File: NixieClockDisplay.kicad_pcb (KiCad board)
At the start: 2 copper layers, 160 x 65 mm, 54 parts, among them U1 TPIC6B595, U2 TPIC6B595, U3 TPIC6B595, U4 TPIC6B595, U5 TPIC6B595, U6 TPIC6B595, U7 WE-FDSM_DC/DC_5V

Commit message: Fiddling.
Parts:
- moved C11 16.0 mm to (130.0, 60.0), turned to 90 degrees
- moved C12 16.0 mm to (170.0, 60.0), turned to 90 degrees
- moved C15 16.0 mm to (180.0, 60.0), turned to 90 degrees
- moved C16 16.0 mm to (220.0, 60.0), turned to 90 degrees
- moved C8 16.0 mm to (120.0, 60.0), turned to 270 degrees
- moved C7 9.62 mm to (80.0, 60.0)
- moved R7 3.40 mm to (78.0, 66.8)
- moved N1 0.36 mm to (90.0, 60.0)
- moved N2 0.36 mm to (110.0, 60.0)
- moved N3 0.36 mm to (140.0, 60.0)
- moved N4 0.36 mm to (160.0, 60.0)
- moved N5 0.36 mm to (190.0, 60.0)
- moved N6 0.36 mm to (210.0, 60.0)
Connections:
- net Net-(J2-Pad1) renamed /HV
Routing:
- net Net-(LED1-Pad3): track 13.7 -> 0.00 mm
- net Net-(N6-Pad1): track 0.00 -> 4.08 mm
- net Net-(N5-Pad1): track 0.00 -> 4.08 mm
- net Net-(N4-Pad1): track 0.00 -> 4.08 mm
- net Net-(N3-Pad1): track 0.00 -> 4.08 mm
- net Net-(N2-Pad1): track 0.00 -> 4.08 mm
- net Net-(N1-Pad1): track 0.00 -> 4.08 mm
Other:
- net class Default: clearance 0.2 -> 0.25
- net class HV added: clearance 2, trace_width 1, via_dia 2, via_drill 1.5
- rule trace_clearance: 0.2 -> 0.25

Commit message: More layout
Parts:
- moved C11 10.3 mm to (140.0, 62.5), turned to 180 degrees
- moved C12 10.3 mm to (160.0, 62.5), turned to 180 degrees
- moved C15 10.3 mm to (190.0, 62.5), turned to 180 degrees
- moved C16 10.3 mm to (210.0, 62.5), turned to 180 degrees
- moved C7 10.3 mm to (90.0, 62.5), turned to 180 degrees
- moved C8 10.3 mm to (110.0, 62.5), turned to 180 degrees
- moved R7 7.65 mm to (79.5, 59.2)
- moved C14 2.00 mm to (175.0, 70.0), turned to 180 degrees
- moved LED8 2.00 mm to (175.0, 65.0), turned to 180 degrees
- moved C10 1.00 mm to (125.0, 70.0), turned to 180 degrees
- moved LED1 0.75 mm to (90.0, 59.2), turned to 180 degrees
- moved LED10 0.75 mm to (210.0, 59.2), turned to 180 degrees
- moved LED2 0.75 mm to (110.0, 59.2), turned to 180 degrees
- moved LED5 0.75 mm to (140.0, 59.2), turned to 180 degrees
- moved LED6 0.75 mm to (160.0, 59.2), turned to 180 degrees
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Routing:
- net +5V: track 0.00 -> 60.7 mm
- net GND: track 0.00 -> 58.2 mm
- net Net-(LED6-Pad1): track 0.00 -> 32.6 mm
- net Net-(LED5-Pad1): track 0.00 -> 20.3 mm
- net Net-(LED10-Pad3): track 0.00 -> 20.3 mm
- net Net-(LED1-Pad1): track 0.00 -> 20.3 mm
- net Net-(LED8-Pad1): track 0.00 -> 16.0 mm
- net Net-(LED4-Pad1): track 0.00 -> 16.0 mm
- net Net-(LED1-Pad3): track 0.00 -> 9.20 mm
- net Net-(LED7-Pad1): track 0.00 -> 7.49 mm
- net Net-(LED3-Pad1): track 0.00 -> 7.49 mm

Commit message: Moar traces
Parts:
- moved R2 15.4 mm to (107.5, 90.0)
- moved R1 15.2 mm to (87.5, 90.0)
- moved C1 5.53 mm to (81.2, 80.0)
- moved C2 5.01 mm to (101.2, 80.0)
- moved U1 5.00 mm to (90.0, 80.0), turned to 90 degrees
- moved U2 5.00 mm to (110.0, 80.0), turned to 90 degrees
- turned U3 to 180 degrees
- turned U4 to 180 degrees
- turned U5 to 180 degrees
- turned U6 to 180 degrees
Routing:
- net GND: track 58.2 -> 86.0 mm, vias 0 -> 16
- net /HOUR_00: track 0.00 -> 22.0 mm, vias 0 -> 1
- net /HOUR_20: track 0.00 -> 17.2 mm
- net Net-(LED6-Pad1): track 32.6 -> 16.3 mm
- net Net-(LED2-Pad1): track 0.00 -> 16.3 mm
- net /HOUR_10: track 0.00 -> 10.8 mm
- added copper zone on B.Cu, net GND
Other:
- net class HV: clearance 2 -> 1

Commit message: More layout
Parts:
- moved R4 11.5 mm to (158.8, 90.0), turned to 0 degrees
- moved R3 10.6 mm to (137.5, 90.0), turned to 0 degrees
- moved R5 10.6 mm to (187.5, 90.0), turned to 0 degrees
- moved R6 10.6 mm to (207.5, 90.0), turned to 0 degrees
- moved C4 10.1 mm to (151.2, 80.0), turned to 270 degrees
- moved C5 10.1 mm to (181.2, 80.0), turned to 270 degrees
- moved C6 10.1 mm to (201.2, 80.0), turned to 270 degrees
- moved C3 9.74 mm to (131.2, 80.0), turned to 270 degrees
- moved U3 4.00 mm to (140.0, 80.0), turned to 90 degrees
- moved U4 4.00 mm to (160.0, 80.0), turned to 90 degrees
- moved U5 4.00 mm to (190.0, 80.0), turned to 90 degrees
- moved U6 4.00 mm to (210.0, 80.0), turned to 90 degrees
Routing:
- net /HOUR_9: track 0.00 -> 38.5 mm, vias 0 -> 1
- net /HOUR_0: track 0.00 -> 26.2 mm, vias 0 -> 1
- net +5V: track 60.7 -> 71.8 mm
- net Net-(R2-Pad2): track 0.00 -> 8.94 mm
- net Net-(R1-Pad2): track 0.00 -> 8.94 mm
- removed copper zone on B.Cu, net GND

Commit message: More layout
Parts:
- added J1: CONN_01X08, Pin_Headers:Pin_Header_Angled_1x08_Pitch2.54mm, B.Cu at (129.5, 94.8)
- added J2: CONN_01X03, Pin_Headers:Pin_Header_Angled_1x03_Pitch2.54mm, B.Cu at (152.4, 94.7)
- added J3: CONN_01X03, Pin_Headers:Pin_Header_Angled_1x03_Pitch2.54mm, B.Cu at (162.6, 94.7)
- U7: moved to B.Cu
- moved U7 32.2 mm to (120.2, 92.5), turned to 180 degrees
- moved R10 24.4 mm to (198.0, 45.6), turned to 90 degrees
- moved R11 24.4 mm to (118.0, 45.6), turned to 90 degrees
- moved R12 24.4 mm to (168.0, 45.6), turned to 90 degrees
- moved R8 24.4 mm to (98.0, 45.6), turned to 90 degrees
- moved R9 24.4 mm to (148.0, 45.6), turned to 90 degrees
- moved R13 20.6 mm to (218.0, 49.4), turned to 90 degrees
- moved R4 2.80 mm to (157.5, 87.5)
- moved R1 2.50 mm to (87.5, 87.5)
- moved R2 2.50 mm to (107.5, 87.5)
- moved R3 2.50 mm to (137.5, 87.5)
- moved R5 2.50 mm to (187.5, 87.5)
- moved R6 2.50 mm to (207.5, 87.5)
- moved C5 1.37 mm to (181.1, 81.4), turned to 90 degrees
- moved C3 1.35 mm to (131.1, 81.3), turned to 90 degrees
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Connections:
- U6 pad 3: /DIN -> Net-(J1-Pad8)
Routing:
- net /HV: track 0.00 -> 237.1 mm
- net +5V: track 71.8 -> 241.9 mm, vias 0 -> 2
- net //G: track 0.00 -> 166.1 mm
- net GND: track 86.0 -> 127.3 mm, vias 16 -> 40
- net /HOUR_9: track 38.5 -> 0.00 mm, vias 1 -> 0
- net +12V: track 0.00 -> 35.5 mm
- net /HOUR_0: track 26.2 -> 0.19 mm, vias 1 -> 0
- net /HOUR_00: track 21.9 -> 0.00 mm, vias 1 -> 0
- net Net-(R6-Pad2): track 0.00 -> 6.88 mm
- net Net-(R5-Pad2): track 0.00 -> 6.88 mm
- net Net-(R4-Pad2): track 0.00 -> 6.88 mm
- net Net-(R3-Pad2): track 0.00 -> 6.88 mm
- net Net-(N6-Pad1): track 4.08 -> 0.00 mm
- net Net-(N5-Pad1): track 4.08 -> 0.00 mm
- net Net-(N4-Pad1): track 4.08 -> 0.00 mm
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- added copper zone on B.Cu, net GND

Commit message: Rotating driver chips
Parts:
- removed REF** (x2): MountingHole_3.7mm, Mounting_Holes:MountingHole_3.7mm
- moved C5 22.1 mm to (198.8, 94.6), turned to 270 degrees
- moved C6 21.4 mm to (218.8, 93.5)
- moved R6 13.5 mm to (221.0, 88.2), turned to 90 degrees
- moved R5 12.5 mm to (200.0, 88.2), turned to 90 degrees
- moved U5 7.50 mm to (190.1, 87.5), turned to 180 degrees
- moved U6 7.50 mm to (210.0, 87.5), turned to 180 degrees
- moved C1 5.25 mm to (81.0, 86.5)
- moved C2 5.25 mm to (100.9, 86.5)
- moved C3 5.25 mm to (131.1, 86.6)
- moved C4 5.25 mm to (150.9, 86.5)
- moved J1 5.25 mm to (129.5, 100.0)
- moved J2 5.25 mm to (152.4, 100.0)
- moved J3 5.25 mm to (162.6, 100.0)
- moved R1 5.25 mm to (87.5, 92.8)
- moved R2 5.25 mm to (107.5, 92.8)
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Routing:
- net +5V: track 241.9 -> 104.5 mm, vias 2 -> 3
- net /HV: track 237.1 -> 328.0 mm
- net /SEC_7: track 0.00 -> 49.7 mm, vias 0 -> 1
- net /SEC_3: track 0.00 -> 31.4 mm, vias 0 -> 2
- net //G: track 166.1 -> 135.7 mm, vias 0 -> 1
- net /SEC_0: track 0.00 -> 29.2 mm, vias 0 -> 1
- net Net-(N1-Pad1): track 0.00 -> 29.0 mm, vias 0 -> 2
- net Net-(N2-Pad1): track 0.00 -> 29.0 mm, vias 0 -> 2
- net Net-(N6-Pad1): track 0.00 -> 29.0 mm, vias 0 -> 2
- net Net-(N5-Pad1): track 0.00 -> 29.0 mm, vias 0 -> 2
- net Net-(N4-Pad1): track 0.00 -> 29.0 mm, vias 0 -> 2
- net Net-(N3-Pad1): track 0.00 -> 29.0 mm, vias 0 -> 2
- net /SEC_2: track 0.00 -> 28.9 mm, vias 0 -> 1
- net /SEC_1: track 0.00 -> 27.1 mm, vias 0 -> 1
- net GND: track 127.3 -> 119.7 mm, vias 40 -> 32
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
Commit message: Much routing
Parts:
- moved C2 17.1 mm to (115.0, 96.2), turned to 0 degrees
- moved C4 17.1 mm to (165.0, 96.2), turned to 0 degrees
- moved C1 17.1 mm to (95.0, 96.2), turned to 0 degrees
- moved C3 16.9 mm to (145.0, 96.2), turned to 0 degrees
- moved R1 12.5 mm to (100.0, 92.5), turned to 90 degrees
- moved R2 12.5 mm to (120.0, 92.5), turned to 90 degrees
- moved R3 12.5 mm to (150.0, 92.5), turned to 90 degrees
- moved R4 12.5 mm to (170.0, 92.5), turned to 90 degrees
- moved C6 4.65 mm to (215.0, 96.2), turned to 0 degrees
- moved R6 4.37 mm to (220.0, 92.5)
- moved R5 4.25 mm to (200.0, 92.5)
- moved C5 4.10 mm to (195.0, 96.2), turned to 0 degrees
- moved U7 2.26 mm to (120.0, 100.0)
- moved U1 2.25 mm to (90.0, 87.5), turned to 180 degrees
- moved U2 2.25 mm to (110.0, 87.5), turned to 180 degrees
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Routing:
- net +5V: track 104.5 -> 509.8 mm, vias 3 -> 0
- net //G: track 135.7 -> 0.00 mm, vias 1 -> 0
- net Net-(J1-Pad8): track 0.00 -> 73.9 mm, vias 0 -> 1
- net /SEC_9: track 0.00 -> 67.6 mm, vias 0 -> 1
- net /SEC_60: track 0.00 -> 65.3 mm, vias 0 -> 1
- net /SEC_8: track 0.00 -> 62.0 mm, vias 0 -> 1
- net /MIN_6: track 0.00 -> 49.6 mm, vias 0 -> 1
- net /SEC_6: track 0.00 -> 49.0 mm, vias 0 -> 1
- net /SEC_50: track 0.00 -> 45.1 mm, vias 0 -> 1
- net /MIN_5: track 0.00 -> 44.6 mm, vias 0 -> 1
- net /SEC_5: track 0.00 -> 40.7 mm, vias 0 -> 1
- net /MIN_4: track 0.00 -> 39.1 mm, vias 0 -> 1
- net /SEC_40: track 0.00 -> 38.0 mm, vias 0 -> 1
- net /MIN_3: track 0.00 -> 34.2 mm, vias 0 -> 1
- net /SEC_4: track 0.00 -> 33.1 mm, vias 0 -> 1
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
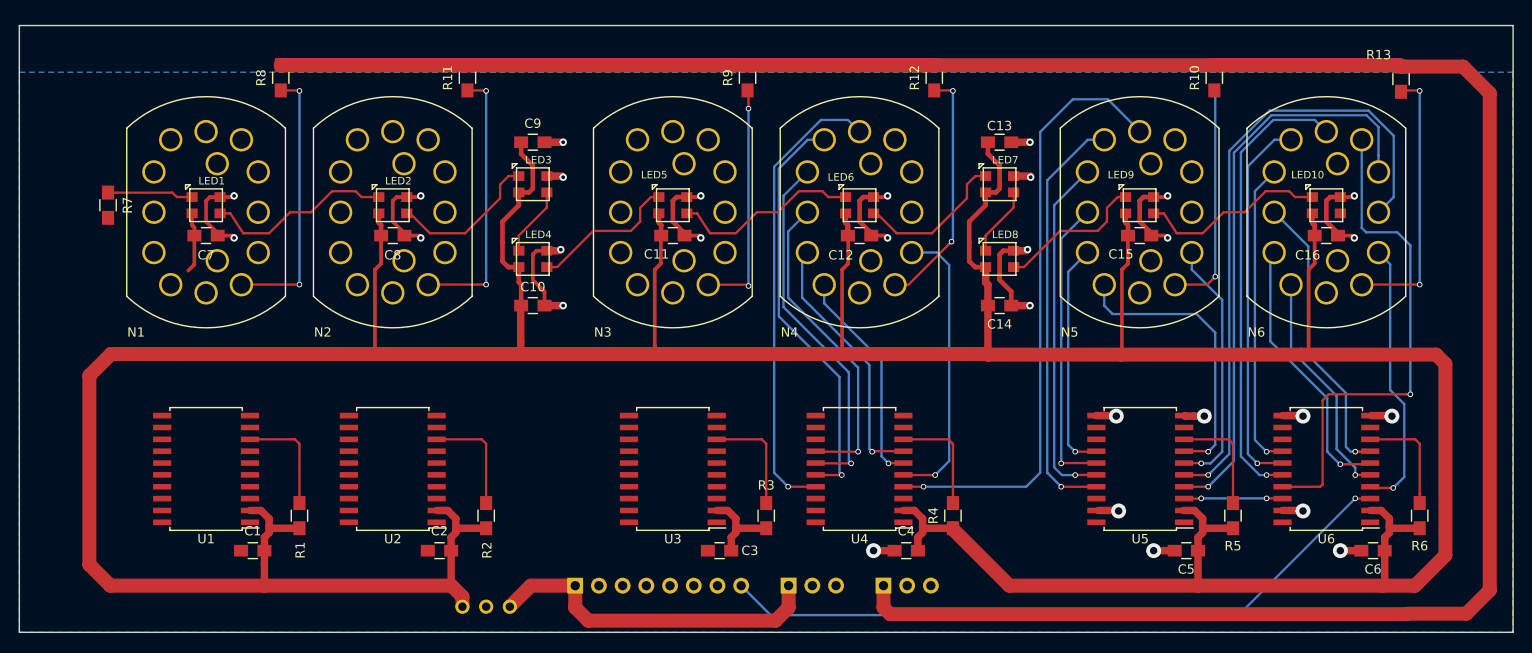
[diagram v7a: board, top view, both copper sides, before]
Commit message: Moved 5V bus.
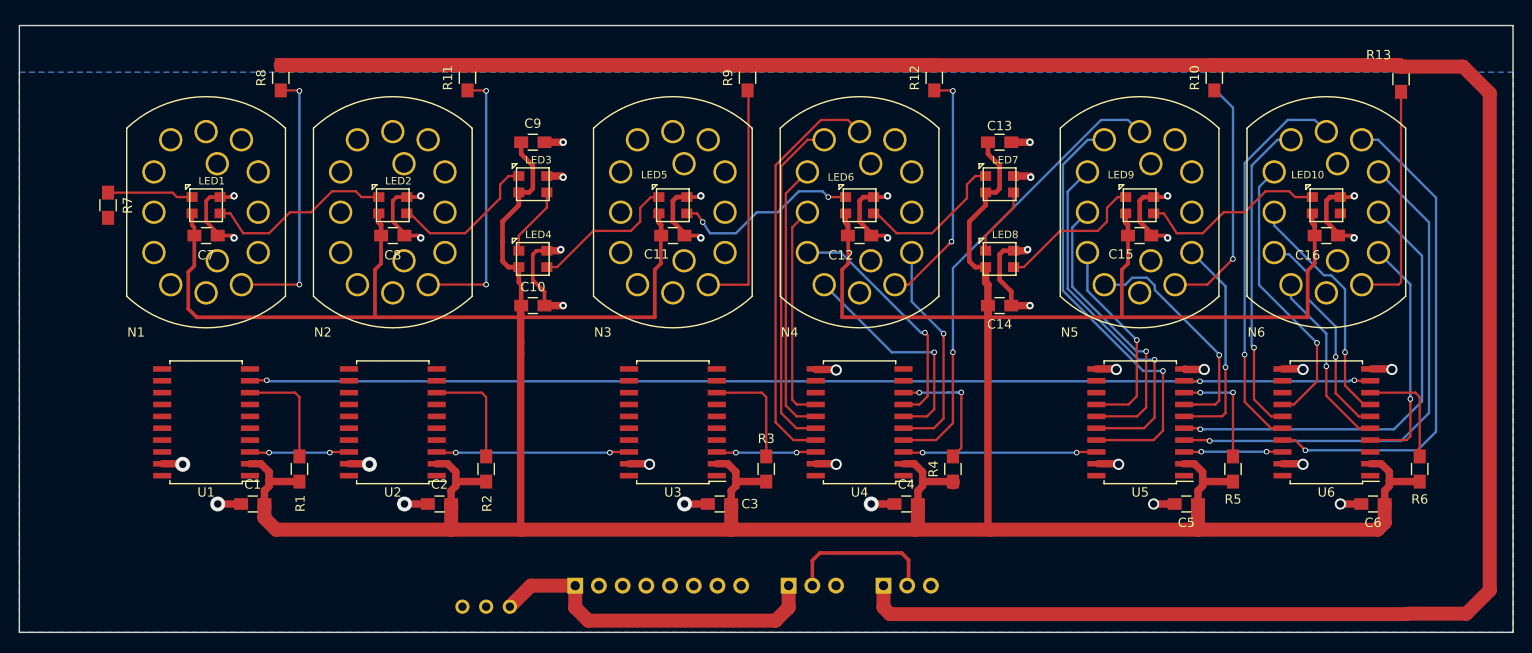
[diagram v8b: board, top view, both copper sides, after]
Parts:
- moved C1 5.00 mm to (95.0, 91.2)
- moved C2 5.00 mm to (115.0, 91.2)
- moved C3 5.00 mm to (145.0, 91.2)
- moved C4 5.00 mm to (165.0, 91.2)
- moved C5 5.00 mm to (195.0, 91.2)
- moved C6 5.00 mm to (215.0, 91.2)
- moved R1 5.00 mm to (100.0, 87.5)
- moved R2 5.00 mm to (120.0, 87.5)
- moved R3 5.00 mm to (150.0, 87.5)
- moved R4 5.00 mm to (170.0, 87.5)
- moved R5 5.00 mm to (200.0, 87.5)
- moved R6 5.00 mm to (220.0, 87.5)
- moved U1 5.00 mm to (90.0, 82.5)
- moved U2 5.00 mm to (110.0, 82.5)
- moved U3 5.00 mm to (140.0, 82.5)
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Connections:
- J1 pad 3: Net-(J1-Pad3) -> GND
- J2 pad 3: Net-(J1-Pad3) -> GND
- J3 pad 2: Net-(J3-Pad2) -> /SHDN
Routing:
- net //G: track 0.00 -> 121.9 mm, vias 0 -> 3
- net Net-(J1-Pad8): track 73.9 -> 0.00 mm, vias 1 -> 0
- net +5V: track 509.8 -> 456.8 mm
- net Net-(U4-Pad3): track 0.00 -> 20.7 mm, vias 0 -> 2
- net Net-(U2-Pad3): track 0.00 -> 20.7 mm, vias 0 -> 2
- net /SEC_9: track 67.6 -> 49.2 mm
- net GND: track 105.8 -> 123.7 mm, vias 29 -> 37
- net /SHDN: track 0.00 -> 16.4 mm
- net /SEC_60: track 65.3 -> 49.8 mm
- net /MIN_3: track 34.2 -> 23.5 mm, vias 1 -> 0
- net Net-(U3-Pad3): track 0.00 -> 10.7 mm, vias 0 -> 2
- net Net-(U1-Pad3): track 0.00 -> 10.7 mm, vias 0 -> 2
- net /MIN_4: track 39.1 -> 29.7 mm, vias 1 -> 0
- net /MIN_5: track 44.6 -> 36.6 mm, vias 1 -> 0
- net /MIN_0: track 31.1 -> 23.9 mm
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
